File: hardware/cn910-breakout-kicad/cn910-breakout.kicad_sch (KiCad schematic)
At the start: 29 parts, among them J1 527461671, J2 USB4125-GF-A-0190_REVA2, J3 PB_RF_OUT, SW1 SW_SPDT, U1 ADA4857-1YRZ

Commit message: PCB work
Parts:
- J1: value 527461671 -> CN910
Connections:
- net USB_5V: no longer D1.2 (A), R_PU1.1
- net VDD: now also D1.2 (A), R_PU1.1
- net PD: now reaches R_LED1.1, R_PU1.2, SW1.1 (A), U1.8 (PD)
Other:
- moved on the sheet: C_VREF_A1, C_VREF_B1, RA1, RB1
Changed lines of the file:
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@@
 	)
 	(rectangle
-		(start 149.86 24.765)
-		(end 202.565 73.66)
+		(start 134.62 51.435)
+		(end 187.325 100.33)
 		(stroke
 			(width 0)
@@
 	(text "Midsupply Bias Network"
 		(exclude_from_sim no)
-		(at 178.054 28.194 0)
+		(at 162.814 54.864 0)
 		(effects
 			(font
@@
 	)
 	(junction
-		(at 156.21 60.96)
+		(at 140.97 87.63)
 		(diameter 0)
 		(color 0 0 0 0)
@@
 	)
 	(junction
-		(at 181.61 45.72)
+		(at 166.37 72.39)
 		(diameter 0)
 		(color 0 0 0 0)
 	)
 	(junction
-		(at 170.18 60.96)
+		(at 154.94 87.63)
 		(diameter 0)
 		(color 0 0 0 0)
@@
 	)
 	(junction
-		(at 156.21 45.72)
+		(at 140.97 72.39)
 		(diameter 0)
 		(color 0 0 0 0)
@@
 	)
 	(junction
-		(at 170.18 45.72)
+		(at 154.94 72.39)
 		(diameter 0)
 		(color 0 0 0 0)
@@
 	(wire
 		(pts
-			(xy 170.18 49.53) (xy 170.18 45.72)
+			(xy 154.94 76.2) (xy 154.94 72.39)
 		)
 		(stroke
@@
 	(wire
 		(pts
-			(xy 170.18 60.96) (xy 156.21 60.96)
+			(xy 154.94 87.63) (xy 140.97 87.63)
 		)
 		(stroke
@@
 	(wire
 		(pts
-			(xy 170.18 45.72) (xy 181.61 45.72)
+			(xy 154.94 72.39) (xy 166.37 72.39)
 		)
 		(stroke
@@
 	(wire
 		(pts
-			(xy 181.61 41.91) (xy 181.61 45.72)
+			(xy 166.37 68.58) (xy 166.37 72.39)
 		)
 		(stroke
@@
 	(wire
 		(pts
-			(xy 181.61 45.72) (xy 187.96 45.72)
+			(xy 166.37 72.39) (xy 172.72 72.39)
 		)
 		(stroke
@@
 	(wire
 		(pts
-			(xy 187.96 49.53) (xy 187.96 45.72)
+			(xy 172.72 76.2) (xy 172.72 72.39)
 		)
 		(stroke
@@
 	(wire
 		(pts
-			(xy 187.96 57.15) (xy 187.96 60.96)
+			(xy 172.72 83.82) (xy 172.72 87.63)
 		)
 		(stroke
@@
 	(wire
 		(pts
-			(xy 187.96 60.96) (xy 170.18 60.96)
+			(xy 172.72 87.63) (xy 154.94 87.63)
 		)
 		(stroke
@@
 	(wire
 		(pts
-			(xy 156.21 45.72) (xy 156.21 49.53)
+			(xy 140.97 72.39) (xy 140.97 76.2)
 		)
 		(stroke
@@
 	(wire
 		(pts
-			(xy 170.18 57.15) (xy 170.18 60.96)
+			(xy 154.94 83.82) (xy 154.94 87.63)
 		)
 		(stroke
@@
 	(wire
 		(pts
-			(xy 156.21 57.15) (xy 156.21 60.96)
+			(xy 140.97 83.82) (xy 140.97 87.63)
 		)
 		(stroke
@@
 	(wire
 		(pts
-			(xy 156.21 29.21) (xy 156.21 34.29)
+			(xy 140.97 55.88) (xy 140.97 60.96)
 		)
 		(stroke
@@
 	(wire
 		(pts
-			(xy 156.21 41.91) (xy 156.21 45.72)
+			(xy 140.97 68.58) (xy 140.97 72.39)
 		)
 		(stroke
@@
 	(wire
 		(pts
-			(xy 156.21 45.72) (xy 170.18 45.72)
+			(xy 140.97 72.39) (xy 154.94 72.39)
 		)
 		(stroke
@@
 	(wire
 		(pts
-			(xy 156.21 60.96) (xy 156.21 63.5)
+			(xy 140.97 87.63) (xy 140.97 90.17)
 		)
 		(stroke
@@
 	)
 	(label "V_{REF}"
-		(at 181.61 41.91 0)
+		(at 166.37 68.58 0)
 		(effects
 			(font
@@
 	)
 	(label "VDD"
-		(at 156.21 29.21 0)
+		(at 140.97 55.88 0)
 		(effects
 			(font
@@
 		)
 	)
+	(label "PD"
+		(at 213.36 116.84 0)
+		(effects
+			(font
+				(size 1.27 1.27)
+			)
+			(justify left bottom)
+		)
+	)
 	(label "EVF_VG"
 		(at 134.62 185.42 270)
@@
 		)
 	)
-	(label "USB_5V"
+	(label "VDD"
 		(at 223.52 81.28 0)
 		(effects
@@
 		(lib_name "GND_3")
 		(lib_id "power:GND")
-		(at 156.21 63.5 0)
+		(at 140.97 90.17 0)
 		(unit 1)
 		(exclude_from_sim no)
@@
 		(fields_autoplaced yes)
 		(property "Reference" "#PWR05"
-			(at 156.21 69.85 0)
+			(at 140.97 96.52 0)
 			(effects
 				(font
@@
 		)
 		(property "Value" "GND"
-			(at 156.21 68.58 0)
+			(at 140.97 95.25 0)
 			(effects
 				(font
@@
 		)
 		(property "Footprint" ""
-			(at 156.21 63.5 0)
+			(at 140.97 90.17 0)
 			(effects
 				(font
@@
 		)
 		(property "Datasheet" ""
-			(at 156.21 63.5 0)
+			(at 140.97 90.17 0)
 			(effects
 				(font
@@
 		)
 		(property "Description" "Power symbol creates a global label with name \"GND\" , ground"
-			(at 156.21 63.5 0)
+			(at 140.97 90.17 0)
 			(effects
 				(font
@@
 	(symbol
 		(lib_id "Device:R")
-		(at 156.21 38.1 0)
+		(at 140.97 64.77 0)
 		(unit 1)
 		(exclude_from_sim no)
@@
 		(fields_autoplaced yes)
 		(property "Reference" "RA1"
-			(at 158.75 36.8299 0)
+			(at 143.51 63.4999 0)
 			(effects
 				(font
@@
 		)
 		(property "Value" "22k"
-			(at 158.75 39.3699 0)
+			(at 143.51 66.0399 0)
 			(effects
 				(font
@@
 		)
 		(property "Footprint" "Resistor_SMD:R_0805_2012Metric_Pad1.20x1.40mm_HandSolder"
-			(at 154.432 38.1 90)
+			(at 139.192 64.77 90)
 			(effects
 				(font
@@
 		)
 		(property "Datasheet" "~"
-			(at 156.21 38.1 0)
+			(at 140.97 64.77 0)
 			(effects
 				(font
@@
 		)
 		(property "Description" "Resistor"
-			(at 156.21 38.1 0)
+			(at 140.97 64.77 0)
 			(effects
 				(font
@@
 	(symbol
 		(lib_id "Device:C")
-		(at 187.96 53.34 180)
+		(at 172.72 80.01 180)
 		(unit 1)
 		(exclude_from_sim no)
@@
 		(fields_autoplaced yes)
 		(property "Reference" "C_VREF_B1"
-			(at 191.77 52.0699 0)
+			(at 176.53 78.7399 0)
 			(effects
 				(font
@@
 		)
 		(property "Value" "100n"
-			(at 191.77 54.6099 0)
+			(at 176.53 81.2799 0)
 			(effects
 				(font
@@
 		)
 		(property "Footprint" "Capacitor_SMD:C_0603_1608Metric_Pad1.08x0.95mm_HandSolder"
-			(at 186.9948 49.53 0)
+			(at 171.7548 76.2 0)
 			(effects
 				(font
@@
 		)
 		(property "Datasheet" "~"
-			(at 187.96 53.34 0)
+			(at 172.72 80.01 0)
 			(effects
 				(font
@@
 		)
 		(property "Description" "Unpolarized capacitor"
-			(at 187.96 53.34 0)
+			(at 172.72 80.01 0)
 			(effects
 				(font
@@
 	(symbol
 		(lib_id "Device:R")
-		(at 156.21 53.34 0)
+		(at 140.97 80.01 0)
 		(unit 1)
 		(exclude_from_sim no)
@@
 		(fields_autoplaced yes)
 		(property "Reference" "RB1"
-			(at 158.75 52.0699 0)
+			(at 143.51 78.7399 0)
 			(effects
 				(font
@@
 		)
 		(property "Value" "22k"
-			(at 158.75 54.6099 0)
+			(at 143.51 81.2799 0)
 			(effects
 				(font
@@
 		)
 		(property "Footprint" "Resistor_SMD:R_0805_2012Metric_Pad1.20x1.40mm_HandSolder"
-			(at 154.432 53.34 90)
+			(at 139.192 80.01 90)
 			(effects
 				(font
@@
 		)
 		(property "Datasheet" "~"
-			(at 156.21 53.34 0)
+			(at 140.97 80.01 0)
 			(effects
 				(font
@@
 		)
 		(property "Description" "Resistor"
-			(at 156.21 53.34 0)
+			(at 140.97 80.01 0)
 			(effects
 				(font
@@
 			)
 		)
-		(property "Value" "527461671"
+		(property "Value" "CN910"
 			(at 41.275 127 0)
 			(effects
@@
 	(symbol
 		(lib_id "Device:C")
-		(at 170.18 53.34 0)
+		(at 154.94 80.01 0)
 		(unit 1)
 		(exclude_from_sim no)
@@
 		(fields_autoplaced yes)
 		(property "Reference" "C_VREF_A1"
-			(at 173.99 52.0699 0)
+			(at 158.75 78.7399 0)
 			(effects
 				(font
@@
 		)
 		(property "Value" "1u"
-			(at 173.99 54.6099 0)
+			(at 158.75 81.2799 0)
 			(effects
 				(font
@@
 		)
 		(property "Footprint" "Capacitor_SMD:C_0603_1608Metric_Pad1.08x0.95mm_HandSolder"
-			(at 171.1452 57.15 0)
+			(at 155.9052 83.82 0)
 			(effects
 				(font
@@
 		)
 		(property "Datasheet" "~"
-			(at 170.18 53.34 0)
+			(at 154.94 80.01 0)
 			(effects
 				(font
@@
 		)
 		(property "Description" "Unpolarized capacitor"
-			(at 170.18 53.34 0)
+			(at 154.94 80.01 0)
 			(effects
 				(font

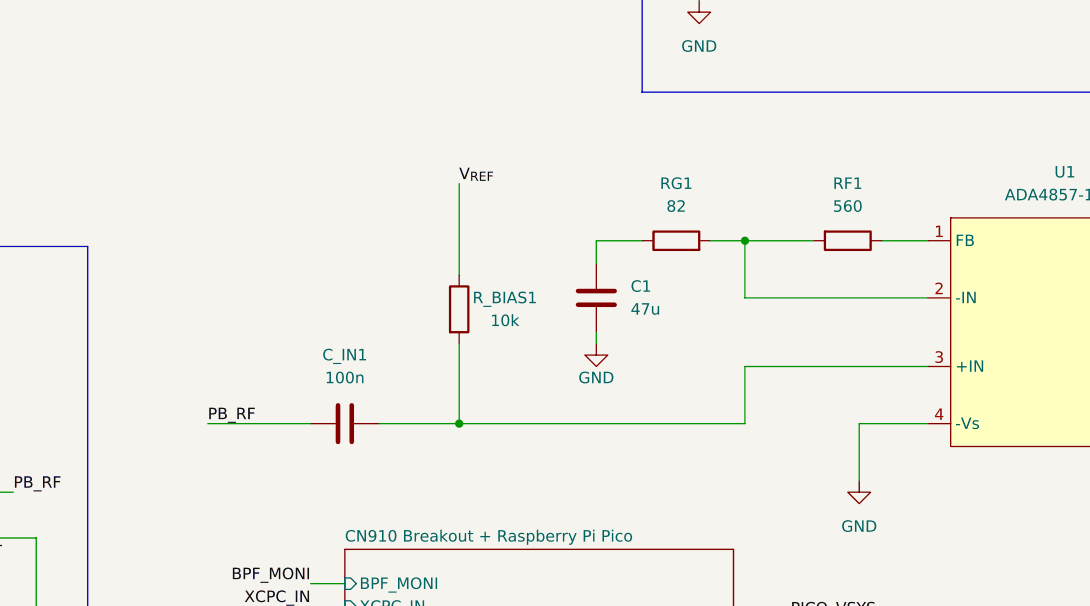
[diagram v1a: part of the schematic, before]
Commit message: Nearly finalized Sony CN910 PCB and added archives of the modified clockgen main board and CX card jig
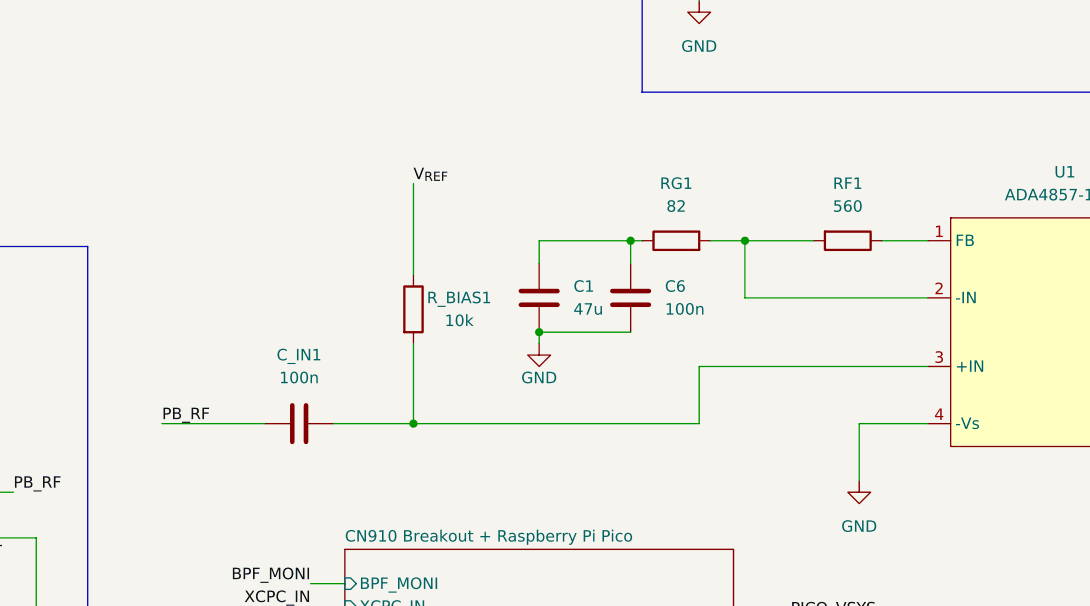
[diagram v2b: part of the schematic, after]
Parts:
- added C6: 100n, Capacitor_SMD:C_0603_1608Metric_Pad1.08x0.95mm_HandSolder, symbol Device:C
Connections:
- net GND: now also C6.2
- net at C1.1, RG1.1: now also C6.1
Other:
- moved on the sheet: C1, C_IN1, R_BIAS1
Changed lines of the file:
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@@
 	)
 	(junction
+		(at 133.35 116.84)
+		(diameter 0)
+		(color 0 0 0 0)
+	)
+	(junction
 		(at 223.52 107.95)
 		(diameter 0)
@@
 	)
 	(junction
-		(at 114.3 137.16)
+		(at 109.22 137.16)
 		(diameter 0)
 		(color 0 0 0 0)
@@
 	)
 	(junction
+		(at 123.19 127)
+		(diameter 0)
+		(color 0 0 0 0)
+	)
+	(junction
 		(at 146.05 116.84)
 		(diameter 0)
@@
 	(wire
 		(pts
-			(xy 146.05 137.16) (xy 146.05 130.81)
+			(xy 140.97 137.16) (xy 140.97 130.81)
 		)
 		(stroke
@@
 	(wire
 		(pts
-			(xy 86.36 137.16) (xy 97.79 137.16)
+			(xy 81.28 137.16) (xy 92.71 137.16)
 		)
 		(stroke
@@
 	(wire
 		(pts
-			(xy 146.05 130.81) (xy 166.37 130.81)
+			(xy 140.97 130.81) (xy 166.37 130.81)
 		)
 		(stroke
@@
 	(wire
 		(pts
+			(xy 133.35 116.84) (xy 133.35 119.38)
+		)
+		(stroke
+			(width 0)
+			(type default)
+		)
+	)
+	(wire
+		(pts
 			(xy 63.5 60.96) (xy 63.5 63.5)
 		)
@@
 	(wire
 		(pts
+			(xy 133.35 116.84) (xy 123.19 116.84)
+		)
+		(stroke
+			(width 0)
+			(type default)
+		)
+	)
+	(wire
+		(pts
 			(xy 45.72 50.8) (xy 63.5 50.8)
 		)
@@
 	(wire
 		(pts
-			(xy 129.54 116.84) (xy 129.54 119.38)
+			(xy 123.19 116.84) (xy 123.19 119.38)
 		)
 		(stroke
@@
 	(wire
 		(pts
+			(xy 123.19 127) (xy 133.35 127)
+		)
+		(stroke
+			(width 0)
+			(type default)
+		)
+	)
+	(wire
+		(pts
 			(xy 140.97 72.39) (xy 140.97 76.2)
 		)
@@
 	(wire
 		(pts
-			(xy 114.3 137.16) (xy 114.3 128.27)
+			(xy 109.22 137.16) (xy 109.22 128.27)
 		)
 		(stroke
@@
 	(wire
 		(pts
-			(xy 114.3 137.16) (xy 146.05 137.16)
+			(xy 109.22 137.16) (xy 140.97 137.16)
 		)
 		(stroke
@@
 	(wire
 		(pts
-			(xy 105.41 137.16) (xy 114.3 137.16)
+			(xy 100.33 137.16) (xy 109.22 137.16)
 		)
 		(stroke
@@
 	(wire
 		(pts
-			(xy 114.3 110.49) (xy 114.3 120.65)
+			(xy 109.22 110.49) (xy 109.22 120.65)
 		)
 		(stroke
@@
 	(wire
 		(pts
-			(xy 134.62 116.84) (xy 129.54 116.84)
+			(xy 134.62 116.84) (xy 133.35 116.84)
 		)
 		(stroke
@@
 	(wire
 		(pts
-			(xy 129.54 127) (xy 129.54 128.27)
+			(xy 123.19 127) (xy 123.19 128.27)
 		)
 		(stroke
@@
 	)
 	(label "V_{REF}"
-		(at 114.3 110.49 0)
+		(at 109.22 110.49 0)
 		(fields_autoplaced yes)
 		(effects
@@
 		)
 		(property "VREF" "2.5V"
-			(at 114.3 111.76 0)
+			(at 109.22 111.76 0)
 			(effects
 				(font
@@
 	)
 	(label "PB_RF"
-		(at 86.36 137.16 0)
+		(at 81.28 137.16 0)
 		(effects
 			(font
@@
 		)
 		(property "V" "~0.4Vpp"
-			(at 86.36 138.43 0)
+			(at 81.28 138.43 0)
 			(effects
 				(font
@@
 		)
 		(property "Fc" "3.579545455KHz"
-			(at 86.36 140.081 0)
+			(at 81.28 140.081 0)
 			(effects
 				(font
@@
 	(symbol
 		(lib_id "Device:R")
-		(at 114.3 124.46 0)
+		(at 109.22 124.46 0)
 		(unit 1)
 		(exclude_from_sim no)
@@
 		(dnp no)
 		(property "Reference" "R_BIAS1"
-			(at 119.38 123.19 0)
+			(at 114.3 123.19 0)
 			(effects
 				(font
@@
 		)
 		(property "Value" "10k"
-			(at 119.38 125.73 0)
+			(at 114.3 125.73 0)
 			(effects
 				(font
@@
 		)
 		(property "Footprint" "Resistor_SMD:R_0805_2012Metric_Pad1.20x1.40mm_HandSolder"
-			(at 112.522 124.46 90)
+			(at 107.442 124.46 90)
 			(effects
 				(font
@@
 		)
 		(property "Datasheet" "~"
-			(at 114.3 124.46 0)
+			(at 109.22 124.46 0)
 			(effects
 				(font
@@
 		)
 		(property "Description" "Resistor"
-			(at 114.3 124.46 0)
+			(at 109.22 124.46 0)
 			(effects
 				(font
@@
 	(symbol
 		(lib_id "Device:C")
-		(at 129.54 123.19 0)
+		(at 123.19 123.19 0)
 		(unit 1)
 		(exclude_from_sim no)
@@
 		(fields_autoplaced yes)
 		(property "Reference" "C1"
-			(at 133.35 121.9199 0)
+			(at 127 121.9199 0)
 			(effects
 				(font
@@
 		)
 		(property "Value" "47u"
-			(at 133.35 124.4599 0)
+			(at 127 124.4599 0)
 			(effects
 				(font
@@
 		)
 		(property "Footprint" "Capacitor_SMD:C_1206_3216Metric_Pad1.33x1.80mm_HandSolder"
-			(at 130.5052 127 0)
+			(at 124.1552 127 0)
 			(effects
 				(font
@@
 		)
 		(property "Datasheet" "~"
-			(at 129.54 123.19 0)
+			(at 123.19 123.19 0)
 			(effects
 				(font
@@
 		)
 		(property "Description" "Unpolarized capacitor"
-			(at 129.54 123.19 0)
+			(at 123.19 123.19 0)
 			(effects
 				(font
@@
 	)
 	(symbol
+		(lib_id "Device:C")
+		(at 133.35 123.19 0)
+		(unit 1)
+		(exclude_from_sim no)
+		(in_bom yes)
+		(on_board yes)
+		(dnp no)
+		(fields_autoplaced yes)
+		(property "Reference" "C6"
+			(at 137.16 121.9199 0)
+			(effects
+				(font
+					(size 1.27 1.27)
+				)
+				(justify left)
+			)
+		)
+		(property "Value" "100n"
+			(at 137.16 124.4599 0)
+			(effects
+				(font
+					(size 1.27 1.27)
+				)
+				(justify left)
+			)
+		)
+		(property "Footprint" "Capacitor_SMD:C_0603_1608Metric_Pad1.08x0.95mm_HandSolder"
+			(at 134.3152 127 0)
+			(effects
+				(font
+					(size 1.27 1.27)
+				)
+				(hide yes)
+			)
+		)
+		(property "Datasheet" "~"
+			(at 133.35 123.19 0)
+			(effects
+				(font
+					(size 1.27 1.27)
+				)
+				(hide yes)
+			)
+		)
+		(property "Description" "Unpolarized capacitor"
+			(at 133.35 123.19 0)
+			(effects
+				(font
+					(size 1.27 1.27)
+				)
+				(hide yes)
+			)
+		)
+		(pin "2"
+		)
+		(pin "1"
+		)
+		(instances
+			(project "cn910-breakout"
+				(path "/f59c37af-48f6-4dd0-89b6-a5866369b568"
+					(reference "C6")
+					(unit 1)
+				)
+			)
+		)
+	)
+	(symbol
 		(lib_id "Device:R")
 		(at 234.95 109.22 180)
@@
 	(symbol
 		(lib_id "Device:C")
-		(at 101.6 137.16 90)
+		(at 96.52 137.16 90)
 		(unit 1)
 		(exclude_from_sim no)
@@
 		(fields_autoplaced yes)
 		(property "Reference" "C_IN1"
-			(at 101.6 129.54 90)
+			(at 96.52 129.54 90)
 			(effects
 				(font
@@
 		)
 		(property "Value" "100n"
-			(at 101.6 132.08 90)
+			(at 96.52 132.08 90)
 			(effects
 				(font
@@
 		)
 		(property "Footprint" "Capacitor_SMD:C_0603_1608Metric_Pad1.08x0.95mm_HandSolder"
-			(at 105.41 136.1948 0)
+			(at 100.33 136.1948 0)
 			(effects
 				(font
@@
 		)
 		(property "Datasheet" "~"
-			(at 101.6 137.16 0)
+			(at 96.52 137.16 0)
 			(effects
 				(font
@@
 		)
 		(property "Description" "Unpolarized capacitor"
-			(at 101.6 137.16 0)
+			(at 96.52 137.16 0)
 			(effects
 				(font
@@
 		(lib_name "GND_6")
 		(lib_id "power:GND")
-		(at 129.54 128.27 0)
+		(at 123.19 128.27 0)
 		(unit 1)
 		(exclude_from_sim no)
@@
 		(dnp no)
 		(property "Reference" "#PWR07"
-			(at 129.54 134.62 0)
+			(at 123.19 134.62 0)
 			(effects
 				(font
@@
 		)
 		(property "Value" "GND"
-			(at 129.54 132.08 0)
+			(at 123.19 132.08 0)
 			(effects
 				(font
@@
 		)
 		(property "Footprint" ""
-			(at 129.54 128.27 0)
+			(at 123.19 128.27 0)
 			(effects
 				(font
@@
 		)
 		(property "Datasheet" ""
-			(at 129.54 128.27 0)
+			(at 123.19 128.27 0)
 			(effects
 				(font
@@
 		)
 		(property "Description" "Power symbol creates a global label with name \"GND\" , ground"
-			(at 129.54 128.27 0)
+			(at 123.19 128.27 0)
 			(effects
 				(font

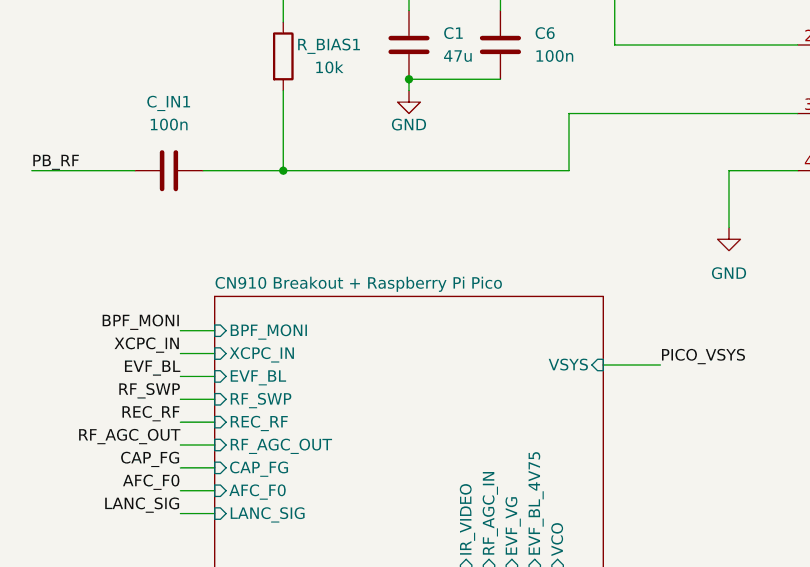
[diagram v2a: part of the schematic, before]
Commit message: Refined routing
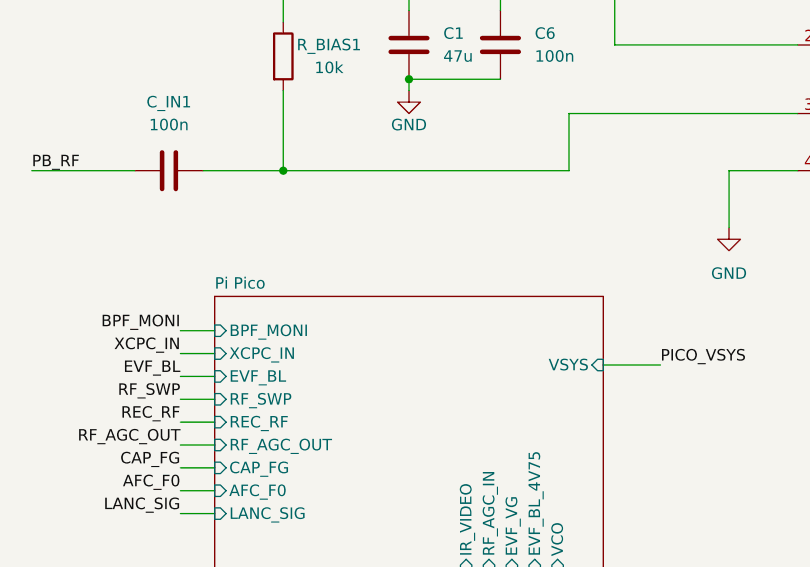
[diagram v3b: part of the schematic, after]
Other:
- sheet CN910 Breakout + Raspberry Pi Pico renamed Pi Pico
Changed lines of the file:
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@@
 	(title_block
 		(title "Sony CCD-TRV615 ADA4857 Amp")
-		(date "2026-04-15")
+		(date "2026-04-28")
 		(rev "1.0")
 		(company "GDH Technologies LLC")
@@
 			(color 0 0 0 0.0000)
 		)
-		(property "Sheetname" "CN910 Breakout + Raspberry Pi Pico"
+		(property "Sheetname" "Pi Pico"
 			(at 101.6 150.4184 0)
 			(effects

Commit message: Refactored CN910 breakout KiCad project files, updating footprint and symbol references to "GDH" naming convention. Adjusted PCB thickness and dielectric properties for improved design accuracy. Added new adhesive layers and updated project metadata with a new variant description. Removed obsolete libraries and 3D models to streamline the project.
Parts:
- J1: footprint CN910 Breakout Footprints:CON_527461671_MOL -> GDH Connectors:CON_527461671_MOL; symbol CN910 Breakout Symbols:CN910_FPC_CON -> GDH Connectors:CN910_FPC_CON
- J2: footprint CN910 Breakout Footprints:GCT_USB4125-GF-A-0190_REVA2 -> GDH Connectors:GCT_USB4125-GF-A-0190_REVA2; symbol USB4125-GF-A-0190_REVA2:USB4125-GF-A-0190_REVA2 -> GDH Connectors:USB4125-GF-A-0190_REVA2
- J3: footprint CN910 Breakout Footprints:Molex_0731000154_BNC_RA_THT -> GDH Connectors:Molex_0731000154_BNC_RA_THT
- SW1: footprint CN910 Breakout Footprints:Slide_Switch_SS12D07_CNK -> GDH Switches:Slide_Switch_SS12D07_CNK
- U1: symbol ada4857:ADA4857-1YRZ -> GDH Amplifiers:ADA4857-1YRZ-R7
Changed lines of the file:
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@@
 			)
 		)
-		(property "Footprint" "CN910 Breakout Footprints:Slide_Switch_SS12D07_CNK"
+		(property "Footprint" "GDH Switches:Slide_Switch_SS12D07_CNK"
 			(at 214.63 105.41 0)
 			(hide yes)
@@
 			)
 		)
-		(property "Footprint" "CN910 Breakout Footprints:Molex_0731000154_BNC_RA_THT"
+		(property "Footprint" "GDH Connectors:Molex_0731000154_BNC_RA_THT"
 			(at 232.41 130.81 0)
 			(hide yes)
@@
 	)
 	(symbol
-		(lib_id "USB4125-GF-A-0190_REVA2:USB4125-GF-A-0190_REVA2")
+		(lib_id "GDH Connectors:USB4125-GF-A-0190_REVA2")
 		(at 33.02 43.18 0)
 		(mirror y)
@@
 			)
 		)
-		(property "Footprint" "CN910 Breakout Footprints:GCT_USB4125-GF-A-0190_REVA2"
+		(property "Footprint" "GDH Connectors:GCT_USB4125-GF-A-0190_REVA2"
 			(at 33.02 43.18 0)
 			(hide yes)
@@
 	)
 	(symbol
-		(lib_id "ada4857:ADA4857-1YRZ")
+		(lib_id "GDH Amplifiers:ADA4857-1YRZ-R7")
 		(at 181.61 127 0)
 		(unit 1)
@@
 	)
 	(symbol
-		(lib_id "CN910 Breakout Symbols:CN910_FPC_CON")
+		(lib_id "GDH Connectors:CN910_FPC_CON")
 		(at 45.72 132.08 0)
 		(unit 1)
@@
 			)
 		)
-		(property "Footprint" "CN910 Breakout Footprints:CON_527461671_MOL"
+		(property "Footprint" "GDH Connectors:CON_527461671_MOL"
 			(at 58.42 127.254 0)
 			(hide yes)
